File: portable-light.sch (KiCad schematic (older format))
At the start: 104 parts, among them J1 Prog, J2 Button, J3 Charger, J4 Seven-segment, J5 LOAD, Q1 MMBT2222A, Q2 MMBT2222A, Q3 MMBT2222A, Q4 MMBT2222A, Q5 MMBT2222A, Q6 PHD45N03LTA, Q7 PHD45N03LTA, Q8 MMBT2222A, U1 L78L05_SOT89, U2 ATmega88PA-AU, U3 LTC1733EMSEPBF, Y1 Crystal

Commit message: divided schematics into multiple sheets moved to arch
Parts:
- removed BT1: Battery_Cell, Connector_PinHeader_2.54mm:PinHeader_1x02_P2.54mm_Vertical, symbol Device:Battery_Cell
- removed C1, C11, C12, C25, C26: 10n, Capacitor_SMD:C_1206_3216Metric_Pad1.42x1.75mm_HandSolder, symbol Device:C_Small
- removed C10, C15, C17, C18, C2, C20, C22, C4, C5, C6, C7, C8, C9: 100n, Capacitor_SMD:C_1206_3216Metric_Pad1.42x1.75mm_HandSolder, symbol Device:C_Small
- removed C13, C14: 15n, Capacitor_SMD:C_1206_3216Metric_Pad1.42x1.75mm_HandSolder, symbol Device:C_Small
- removed C16, C19: 300n, Capacitor_SMD:C_0805_2012Metric_Pad1.15x1.40mm_HandSolder, symbol Device:C_Small
- removed C23, C24: 22p, Capacitor_SMD:C_1206_3216Metric_Pad1.42x1.75mm_HandSolder, symbol Device:C_Small
- removed C27: 330n, Capacitor_SMD:C_1206_3216Metric_Pad1.42x1.75mm_HandSolder, symbol Device:C_Small
- removed C28, C3: 10u, Capacitor_THT:C_Radial_D5.0mm_H7.0mm_P2.00mm, symbol Device:C_Small
- removed D1, D2, D3, D4, D5, D6, D7: 1N5819, Diode_SMD:D_SMA_Handsoldering, symbol Diode:1N5819
- removed D8, D9: 1N5819, Diode_THT:D_DO-41_SOD81_P12.70mm_Horizontal, symbol Diode:1N5819
- removed J1: Prog, Connector_PinHeader_2.54mm:PinHeader_1x05_P2.54mm_Vertical, symbol Connector_Generic:Conn_01x05
- removed J2: Button, Ribbon_Cable:Ribbon_2, symbol Connector_Generic:Conn_01x02
- removed J4: Seven-segment, Ribbon_Cable:Ribbon_8, symbol Connector_Generic:Conn_01x08
- removed J5: LOAD, Connector_PinHeader_2.54mm:PinHeader_1x02_P2.54mm_Vertical, symbol Device:LED
- removed JP1: SolderJumper_2_Open, Jumper:SolderJumper-2_P1.3mm_Open_TrianglePad1.0x1.5mm, symbol Jumper:SolderJumper_2_Open
- removed JP2: Jumper_2_Open, Jumper:SolderJumper-2_P1.3mm_Open_RoundedPad1.0x1.5mm, symbol Jumper:Jumper_2_Open
- removed L1: 22u, Capacitor_THT:CP_Radial_D8.0mm_P5.00mm, symbol Device:L
- removed NT1, NT2: Net-Tie_2, NetTie:NetTie-2_SMD_Pad0.5mm, symbol Device:Net-Tie_2
- removed Q1, Q2, Q3, Q4, Q5, Q8: MMBT2222A, Package_TO_SOT_SMD:SOT-23, symbol Transistor_BJT:MMBT3904
- removed Q6, Q7: PHD45N03LTA, UniX_Generic:DPAK, symbol PHD45N03LTA:PHD45N03LTA
- removed R1, R4: 1k, Resistor_SMD:R_0603_1608Metric_Pad1.05x0.95mm_HandSolder, symbol Device:R_Small
- removed R10, R11, R12, R13, R14, R15, R16, R41, R42: 475R, Resistor_SMD:R_1206_3216Metric_Pad1.42x1.75mm_HandSolder, symbol Device:R_Small
- removed R17, R18, R19, R2, R21, R24, R25, R37, R38, R39, R43, R6, R8: 1K, Resistor_SMD:R_0603_1608Metric_Pad1.05x0.95mm_HandSolder, symbol Device:R_Small
- removed R20: 500K, Resistor_THT:R_Axial_DIN0309_L9.0mm_D3.2mm_P12.70mm_Horizontal, symbol Device:R_Small
- removed R22, R23, R3, R7, R9: 33R, Resistor_SMD:R_0805_2012Metric_Pad1.15x1.40mm_HandSolder, symbol Device:R_Small
- removed R26: 1R60, Resistor_SMD:R_0805_2012Metric_Pad1.15x1.40mm_HandSolder, symbol Device:R_Small
- removed R27, R28, R30, R31, R32, R33, R35, R36, R5: 56R, Resistor_SMD:R_0805_2012Metric_Pad1.15x1.40mm_HandSolder, symbol Device:R_Small
- removed R29, R34: 100R, Resistor_SMD:R_1206_3216Metric_Pad1.42x1.75mm_HandSolder, symbol Device:R_Small
- removed R40: 10K, Resistor_SMD:R_1206_3216Metric_Pad1.42x1.75mm_HandSolder, symbol Device:R_Small
- removed R44: 475R, Resistor_SMD:R_0805_2012Metric_Pad1.15x1.40mm_HandSolder, symbol Device:R_Small
- removed U1: L78L05_SOT89, Package_TO_SOT_SMD:SOT-89-3, symbol Regulator_Linear:L78L05_SOT89
- removed U2: ATmega88PA-AU, Package_QFP:TQFP-32_7x7mm_P0.8mm, symbol MCU_Microchip_ATmega:ATmega88PA-AU
- removed U3: LTC1733EMSEPBF, UniX_Generic:MSOP-10_MSE, symbol LTC1733:LTC1733EMSEPBF
- removed Y1: Crystal, Crystal:Crystal_SMD_HC49-SD, symbol Device:Crystal
- added BT1: Battery_Cell, Connector_PinHeader_2.54mm:PinHeader_1x02_P2.54mm_Vertical, symbol portable-light-rescue:Battery_Cell-Device
- added C17: 100n, Capacitor_SMD:C_1206_3216Metric_Pad1.42x1.75mm_HandSolder, symbol portable-light-rescue:C_Small-Device
- added C27: 330n, Capacitor_SMD:C_1206_3216Metric_Pad1.42x1.75mm_HandSolder, symbol portable-light-rescue:C_Small-Device
- added D8, D9: 1N5819, Diode_THT:D_DO-41_SOD81_P12.70mm_Horizontal, symbol portable-light-rescue:1N5819-Diode
- added NT1, NT2: Net-Tie_2, NetTie:NetTie-2_SMD_Pad0.5mm, symbol portable-light-rescue:Net-Tie_2-Device
- added R26: 1R60, Resistor_SMD:R_0805_2012Metric_Pad1.15x1.40mm_HandSolder, symbol portable-light-rescue:R_Small-Device
- added U1: L78L05_SOT89, Package_TO_SOT_SMD:SOT-89-3, symbol portable-light-rescue:L78L05_SOT89-Regulator_Linear
- C21: symbol Device:C_Small -> portable-light-rescue:C_Small-Device
- J3: symbol Connector_Generic:Conn_01x02 -> portable-light-rescue:Conn_01x02-Connector_Generic
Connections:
- net +15V: now also U1.3 (IN)
- net +BATT: now also BT1.1 (+), C27.1, D9.2 (A)
- net GND: now also NT1.1, NT2.1
- net GNDA: now also NT2.2
- net GNDPWR: now also BT1.2 (-), C17.2, NT1.2, R26.2, U1.2 (GND)
- net VBUS: now also D8.1 (K), D9.1 (K)
- new net: C17.1, D8.2 (A), U1.1 (OUT)
- new net: C27.2, R26.1
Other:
- note removed: "Buck converter"
- note removed: "Charge controller"
- note removed: "Charge pump"
- note removed: "DO NOT PLACE"
- note removed: "MUST SOLDER JUMPER"
- note removed: "Microcontroller"
- note removed: "Req=18.6R"
- moved on the sheet: C21, J3

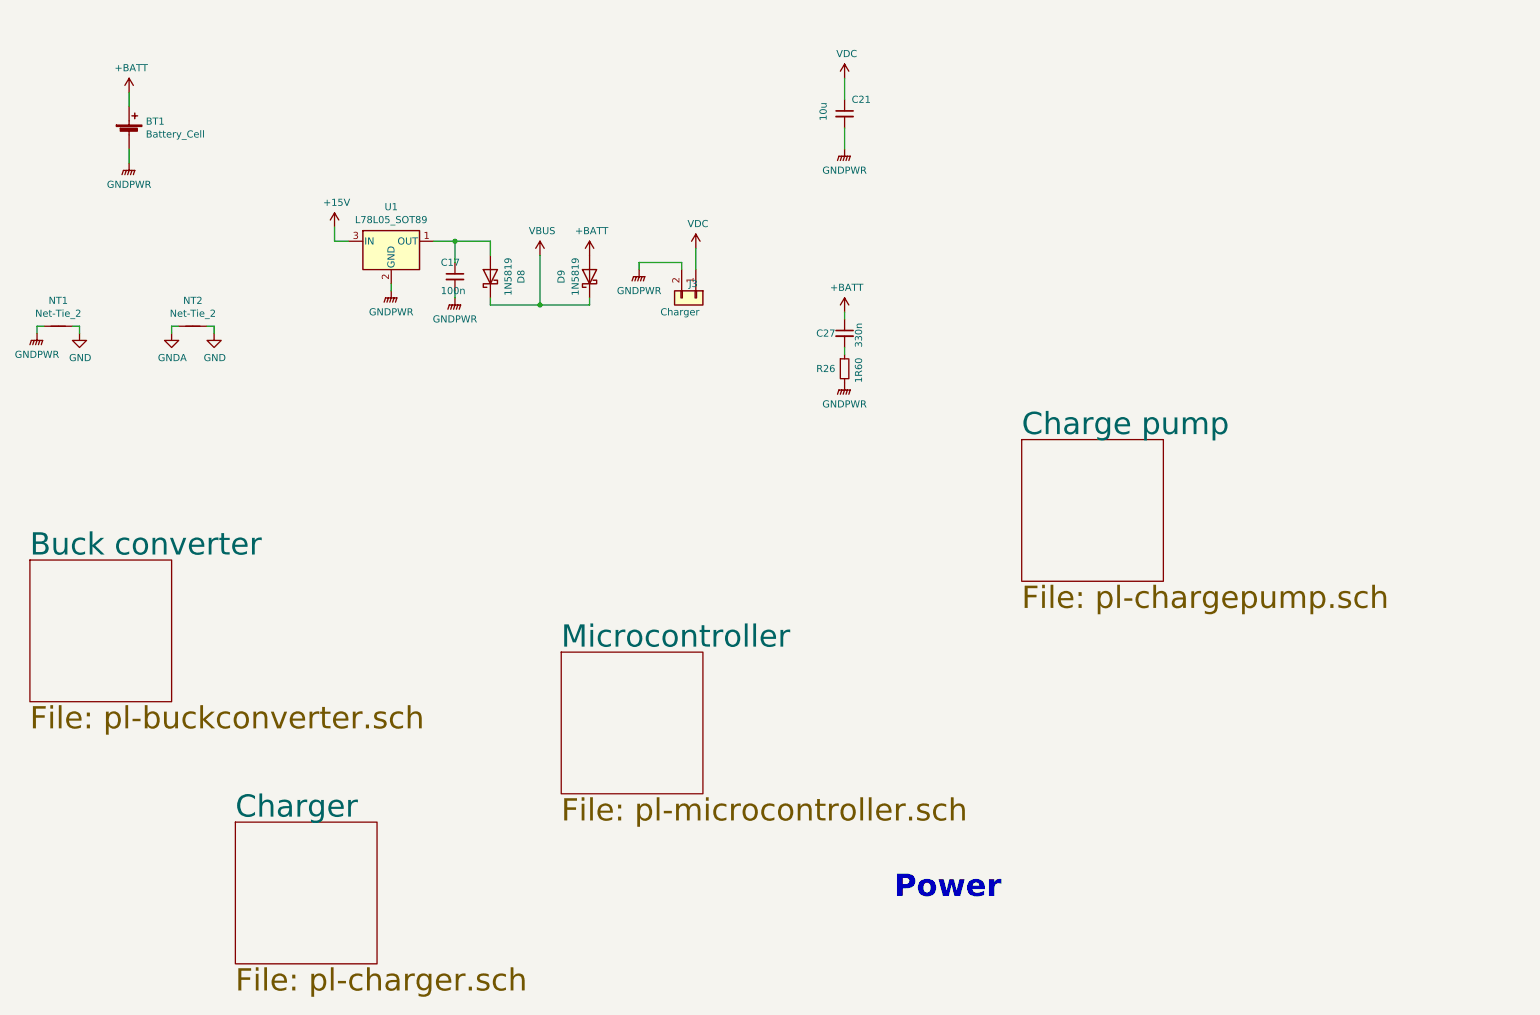
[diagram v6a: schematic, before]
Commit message: Fixed hierarchical sheet for microcontroller unit
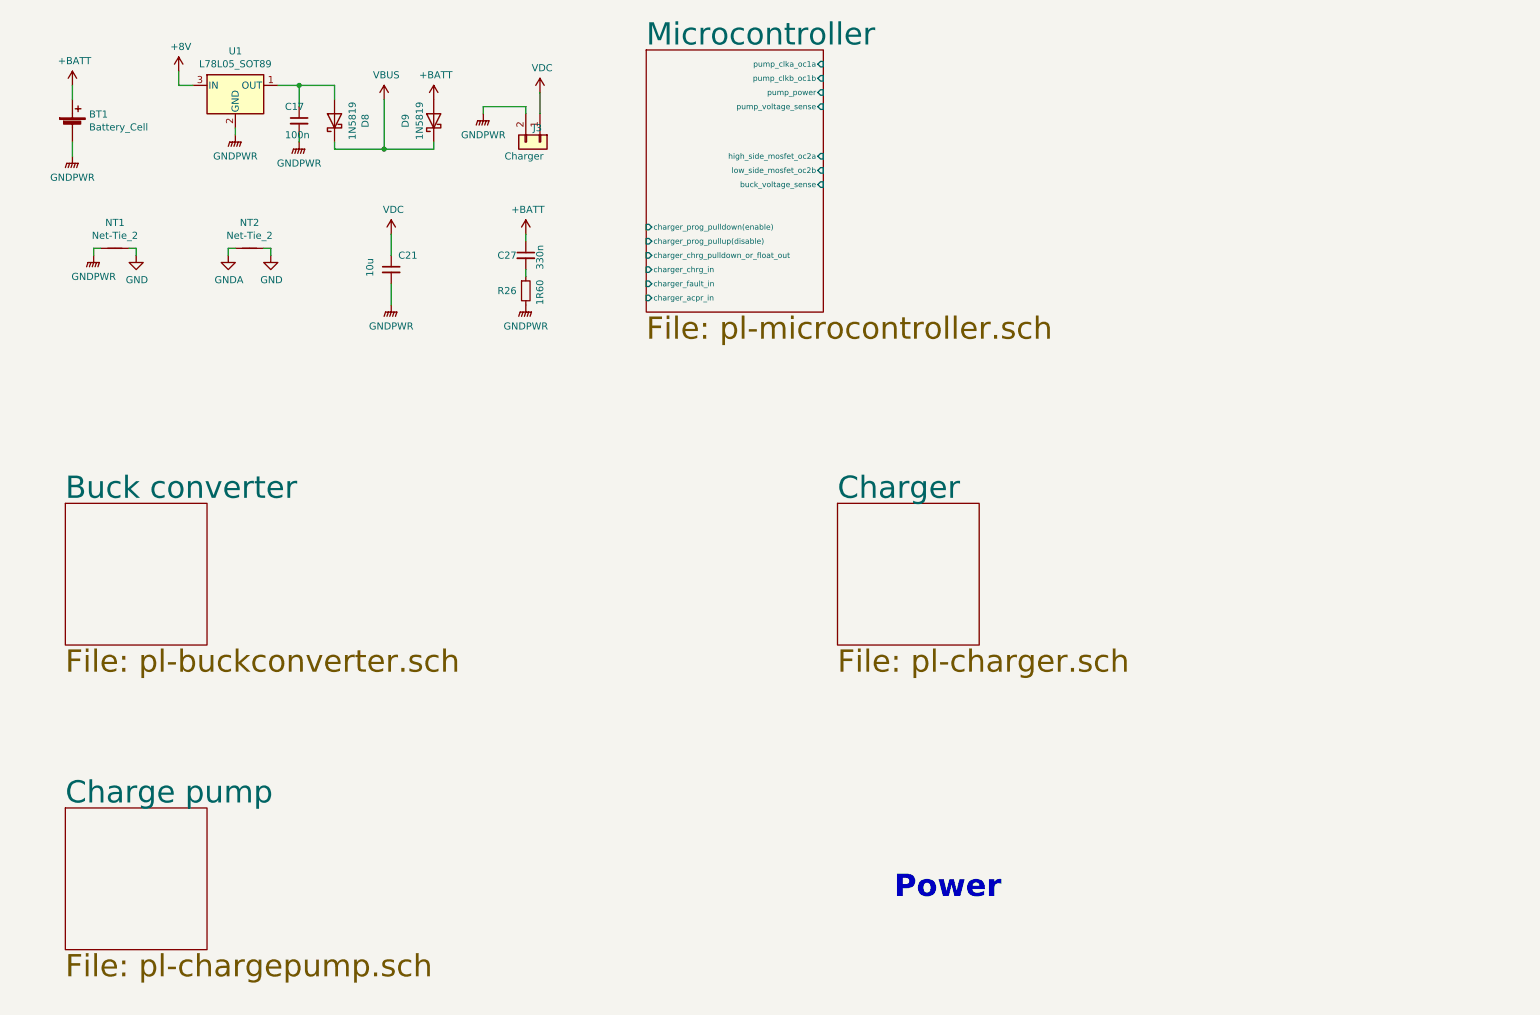
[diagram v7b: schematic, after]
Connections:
- net +15V renamed +8V
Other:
- moved on the sheet: BT1, C17, C21, C27, D8, D9, J3, NT1, NT2, R26, U1

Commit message: Charger hierarchical sheet fixed
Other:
- moved on the sheet: BT1, C17, C21, C27, D8, D9, J3, NT1, NT2, R26, U1
